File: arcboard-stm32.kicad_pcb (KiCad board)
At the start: 2 copper layers, 59.5 x 59.7 mm, 85 parts, among them J1 Conn_01x04_Socket, J10 Conn_01x04_Socket, J13 FFC05001-12SBA124W5M, J14 FFC05001-12SBA124W5M, J15 FFC05001-12SBA124W5M, J16 FFC05001-12SBA124W5M, J2 Conn_01x04_Socket, J3 FFC05001-12SBA124W5M, J4 FFC05001-12SBA124W5M, J5 Conn_01x02_Socket, J6 FFC05001-12SBA124W5M, J7 FFC05001-12SBA124W5M, J8 FFC05001-12SBA124W5M, J9 Conn_01x03_Socket, U1 XC6210B332MR-G, U10 1N4148W_C81598, U11 W25Q16JVSSIQTR, U13 2N7002, U15 TS-1187A-B-A-B, U2 TYPE-C-31-M-13, U3 STM32F405RGTx, U4 2N7002, U5 BAV70S,115, U6 BAV70S,115, U7 BAV70S,115, U8 BAV70S,115, U9 BAV70S,115, Y1 Crystal_GND24

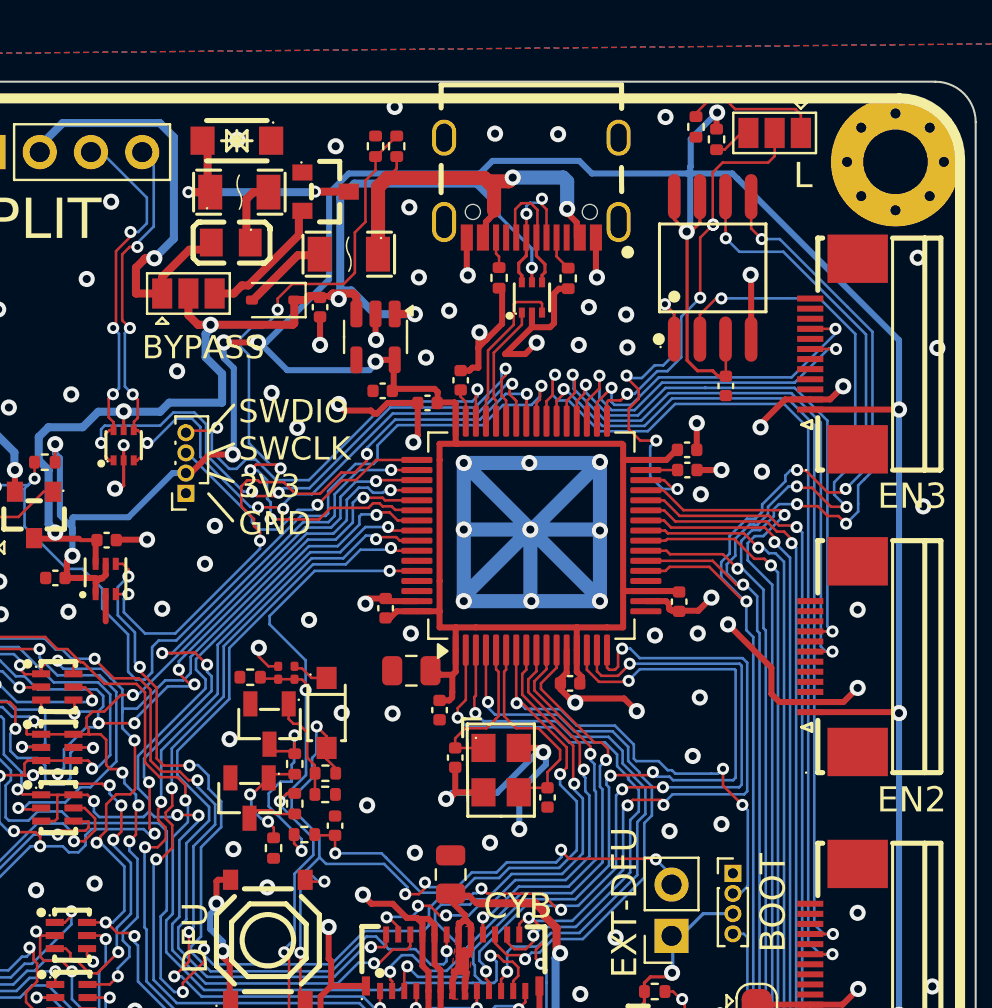
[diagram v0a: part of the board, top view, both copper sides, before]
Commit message: adding spare pins, more routing
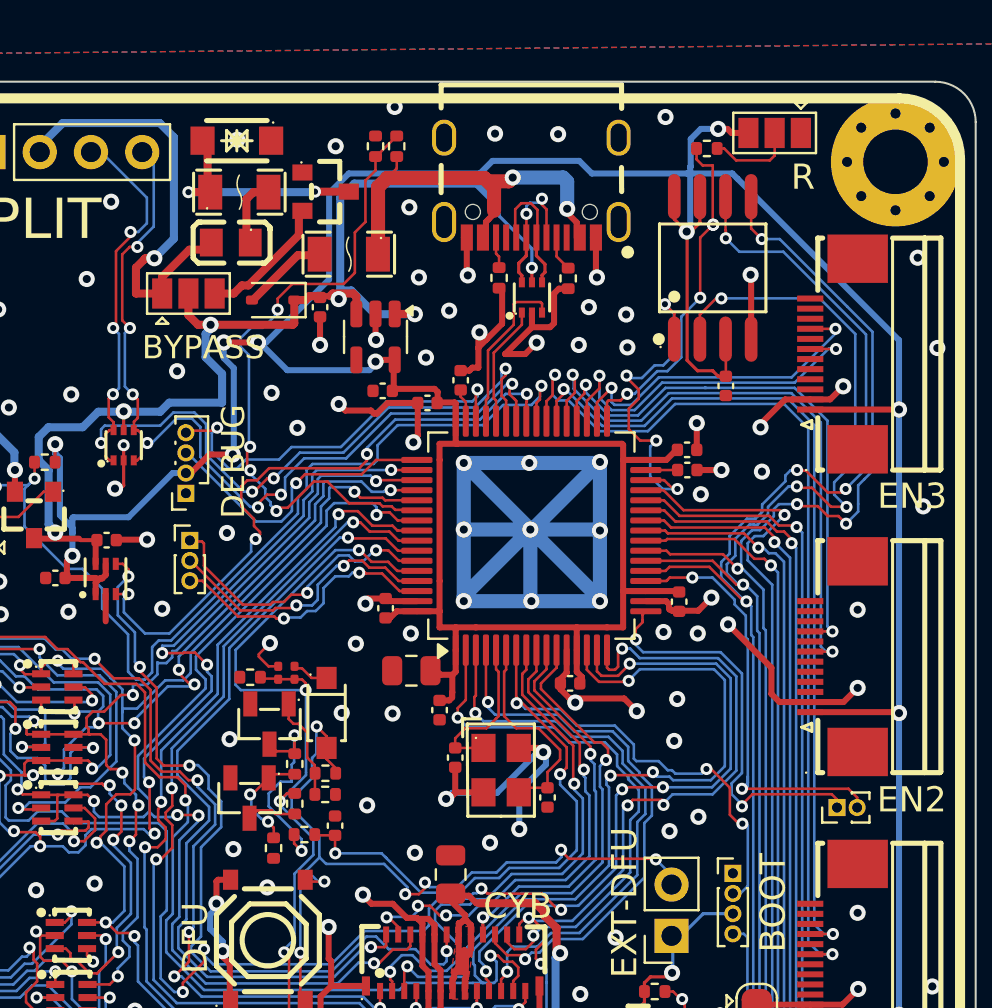
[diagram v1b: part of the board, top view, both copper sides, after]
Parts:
- removed R20: 10k, Resistor_SMD:R_0402_1005Metric
- added J11: Conn_01x02_Socket, Connector_PinHeader_1.00mm:PinHeader_1x02_P1.00mm_Vertical, F.Cu at (115.2, 98.5)
- added J12: Conn_01x03_Socket, Connector_PinHeader_1.00mm:PinHeader_1x03_P1.00mm_Vertical, F.Cu at (83.1, 85.2)
- moved R12 1.20 mm to (108.7, 65.8), turned to 180 degrees
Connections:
- JP3 pad 1: Net-(JP3-A) -> GND
- JP3 pad 2: SPLIT_HAND -> Net-(JP3-C)
- JP3 pad 3: Net-(JP3-B) -> +3V3
- R12 pad 1: GND -> Net-(JP3-C)
- R12 pad 2: Net-(JP3-A) -> SPLIT_HAND
- U3 pad 17: unconnected-(U3-PA3-Pad17) -> SPARE4
- U3 pad 20: unconnected-(U3-PA4-Pad20) -> SPARE5
- U3 pad 59: unconnected-(U3-PB7-Pad59) -> SPARE1
- U3 pad 61: unconnected-(U3-PB8-Pad61) -> SPARE2
- U3 pad 62: unconnected-(U3-PB9-Pad62) -> SPARE3
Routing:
- net SPARE5: track 0.00 -> 21.6 mm, vias 0 -> 2
- net SPARE4: track 0.00 -> 20.3 mm, vias 0 -> 2
- net SPARE1: track 0.00 -> 15.0 mm, vias 0 -> 2
- net SPARE2: track 0.00 -> 14.2 mm, vias 0 -> 2
- net SPARE3: track 0.00 -> 13.8 mm, vias 0 -> 2
- net Net-(JP3-A): track 6.86 -> 0.00 mm
- net BOOT0: track 90.6 -> 95.0 mm
- net Net-(JP3-C): track 0.00 -> 4.31 mm
- net SPLIT_HAND: track 20.1 -> 17.3 mm
- net VBUS_DETECT: track 35.0 -> 32.7 mm
- net ROW6: track 78.9 -> 76.8 mm
- net Net-(JP3-B): track 1.92 -> 0.00 mm
- net ROW5: track 128.4 -> 126.4 mm
- net ROW4: track 83.1 -> 81.4 mm
- net COL9: track 66.9 -> 68.3 mm
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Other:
- board text added: "DEBUG"
- board text added: "GND 3V3 SWCLK SWDIO"
- board text added: "R"
- board text removed: "L"
- board text removed: "SWDIO SWCLK 3V3 GND"

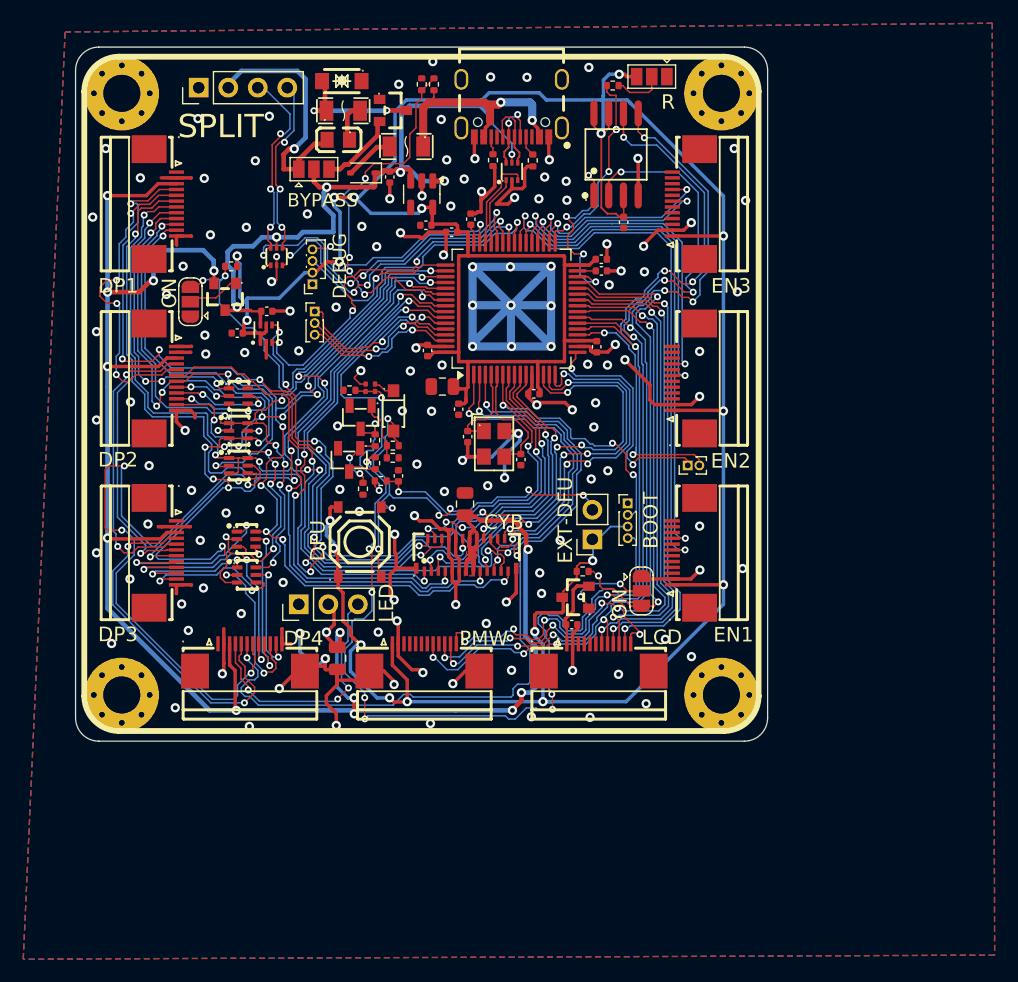
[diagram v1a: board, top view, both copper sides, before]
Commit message: silkscreen updates
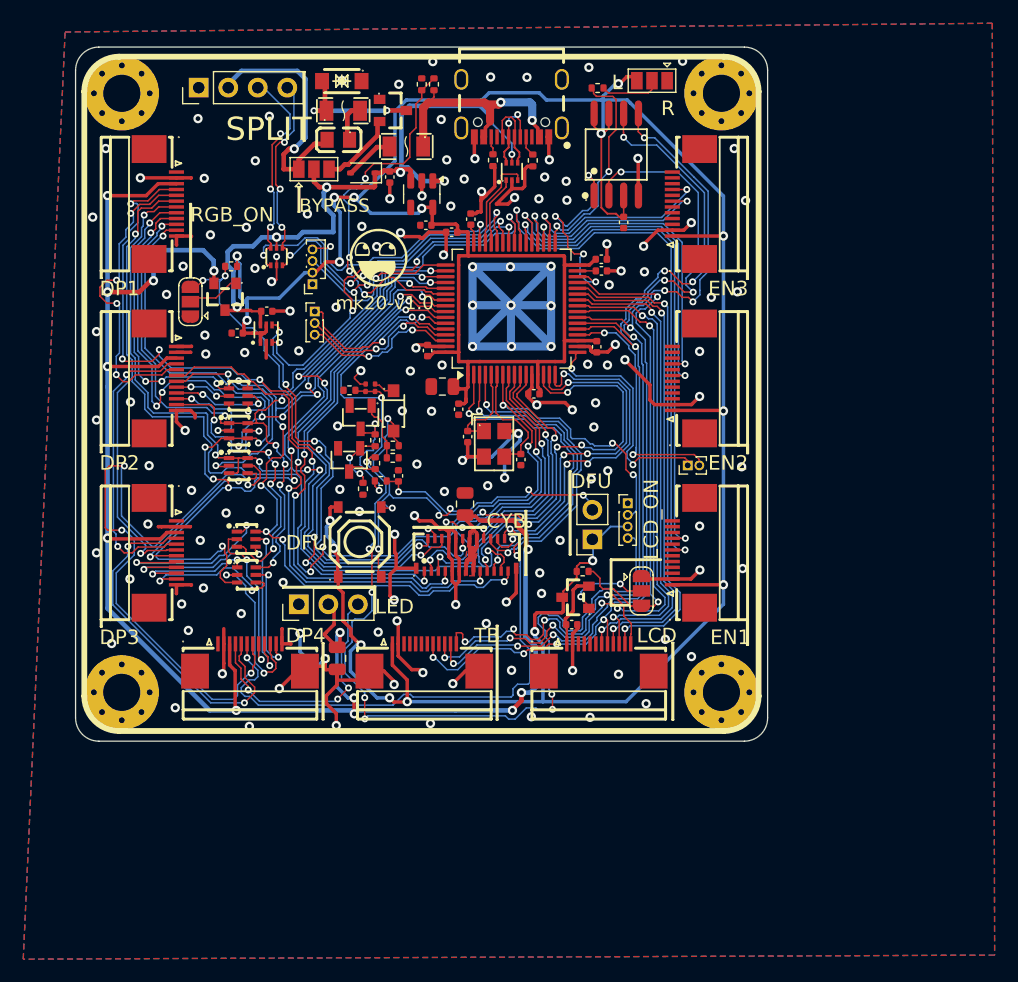
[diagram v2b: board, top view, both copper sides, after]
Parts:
- removed U11: W25Q16JVSSIQTR, kicad-libraries:SOIC-8_L5.3-W5.3-P1.27-LS8.0-BL
- added LOGO1: **REF, kicad-libraries:awesome-logo, B.Cu at (72.9, 95.7)
- added LOGO2: **REF, kicad-libraries:awesome-logo, F.Cu at (88.6, 80.6)
- added LOGO3: **REF, kicad-libraries:cyboard-logo-10mm, B.Cu at (96.2, 109.3)
- added LOGO4: **REF, kicad-libraries:qmk-lite, B.Cu at (105.1, 87.4)
- added U14: W25Q128JVSIQTR, kicad-libraries:SOIC-8_L5.3-W5.3-P1.27-LS8.0-BL, F.Cu at (109.0, 71.7)
- moved R12 1.32 mm to (107.4, 66.0)
- moved JP3 0.35 mm to (112.1, 65.4)
- moved H3 0.22 mm to (118.0, 118.0)
- moved H4 0.22 mm to (66.5, 118.0)
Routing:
- net ENCODER3_R2: track 16.8 -> 18.6 mm
- net GND: track 232.2 -> 234.0 mm, vias 141 -> 145
- net ENCODER2_R2: track 27.8 -> 29.4 mm
- net FLASH_CS: track 17.4 -> 19.0 mm
- net +3V3: track 290.9 -> 289.4 mm, vias 19 -> 18
- net ENCODER1_R1: track 46.1 -> 47.5 mm
- net COL10: track 96.8 -> 95.4 mm, vias 12 -> 11
- net ENCODER3_R1: track 18.1 -> 16.9 mm
- net RGB_ON: track 47.5 -> 48.7 mm
- net SPLIT_HAND: track 17.3 -> 18.5 mm, vias 4 -> 2
- net SPI1_CLK: track 87.6 -> 86.5 mm, vias 9 -> 8
- net ENCODER2_R1: track 30.2 -> 31.3 mm
- net Net-(JP3-C): track 4.31 -> 5.23 mm
- net Net-(J8-MOSI): track 14.8 -> 14.2 mm, vias 3 -> 2
- net LCD_ON: vias 3 -> 2
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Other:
- board text added: "51.55mm between holes"
- board text added: "59.5mm edge width"
- board text added: "59.7mm edge height"
- board text added: "DFU 3V3"
- board text added: "DO 5V GND"
- board text added: "GND NRST 3V3 BOOT0"
- board text added: "L"
- board text added: "LCD_ON"
- board text added: "LED-DO"
- board text added: "RGB_ON"
- board text added: "SPARE1 SPARE2 SPARE3"
- board text added: "SPARE5 SPARE4"
- board text added: "STM32-INATOR"
- board text added: "SWDIO SWCLK 3V3 GND"
- board text added: "TB"
- board text added: "mk20-v1.0"
- board text removed: "BOOT"
- board text removed: "DEBUG"
- board text removed: "DP1 = Dpad DP2-4 = Paddle EN1-2 = Top wheel encoders EN3 = Ring encoder CYB = Cyboard 25-pin LED = Gnd, +5v, WS2812 data ON = solder these for normal operation; else bypass EXT-DFU = activate DFU from external switch RESET = activate nRST from external switch BYPASS = solder arrow side to bypass R/L = handedness"
- board text removed: "EXT-DFU"
- board text removed: "GND 3V3 SWCLK SWDIO"
- board text removed: "ON"
- board text removed: "PMW"

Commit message: silkscreen improvements
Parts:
- added LOGO5: **REF, kicad-libraries:arcboard-stm32-qr-code-10x10, B.Cu at (115.3, 80.2)
- added LOGO6: **REF, kicad-libraries:cyboard-logo-5mm, F.Cu at (93.0, 102.2)
- moved LOGO3 30.6 mm to (106.6, 80.5)
- moved LOGO1 6.48 mm to (67.3, 92.4)
- moved LOGO2 5.91 mm to (88.9, 86.5)
- moved LOGO4 3.83 mm to (108.9, 87.1)
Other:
- board text added: "128MB"
- board text added: "STM32F405"

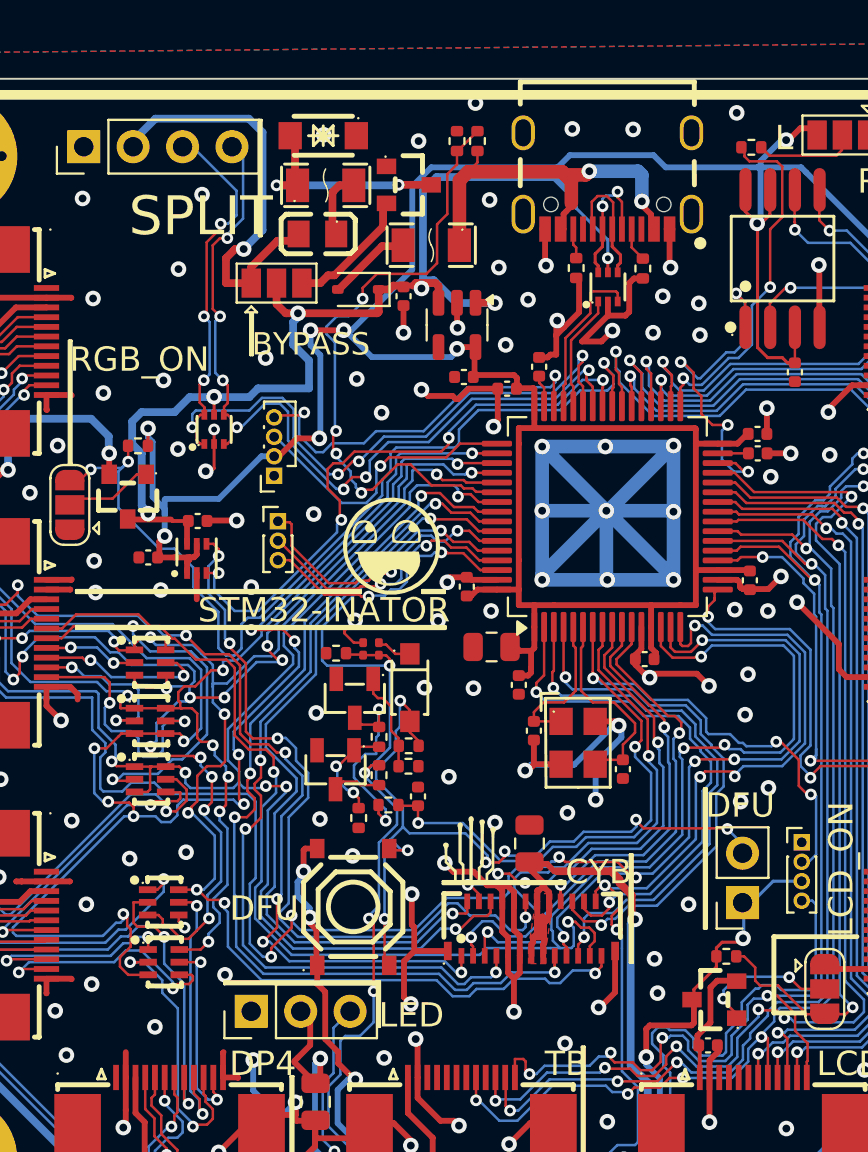
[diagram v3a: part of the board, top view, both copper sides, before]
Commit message: moved a few items, silkscreen improvements
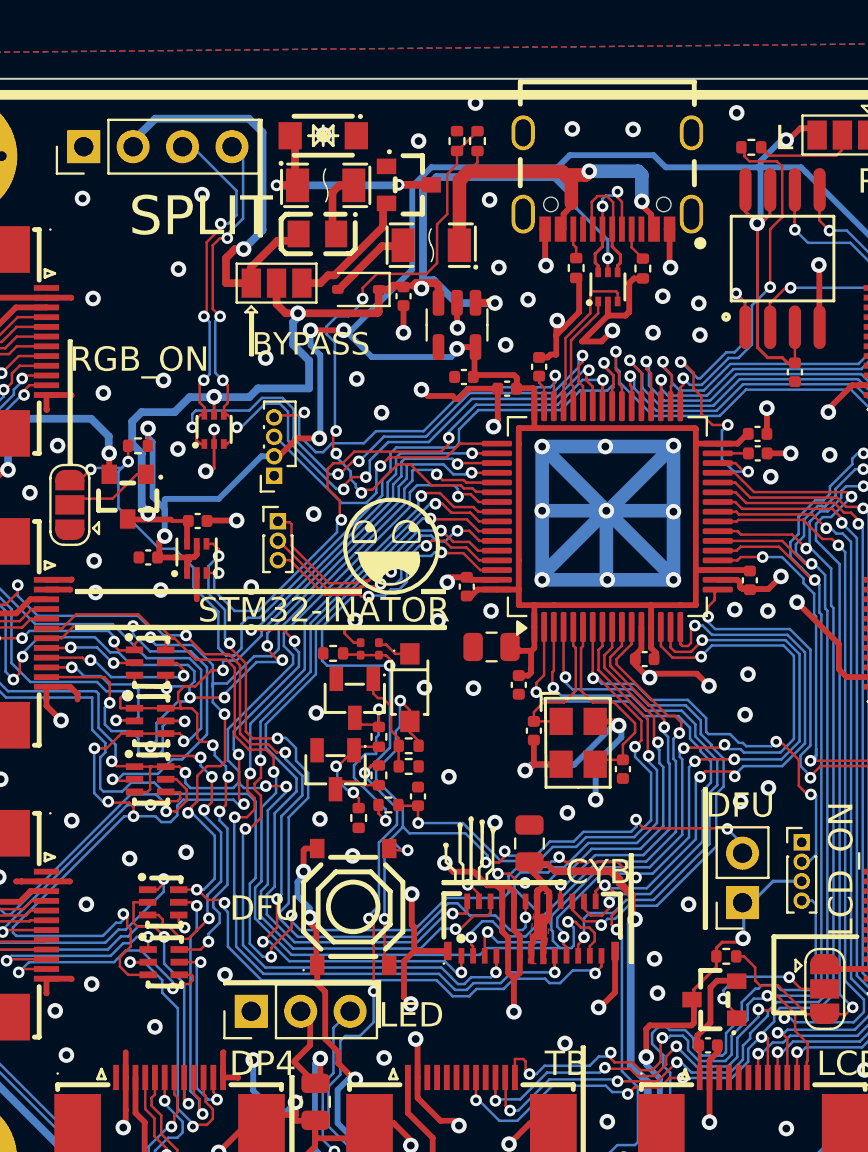
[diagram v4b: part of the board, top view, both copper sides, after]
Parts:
- removed R13: 0402WGF1002TCE, Resistor_SMD:R_0402_1005Metric
- added LOGO7: **REF, kicad-libraries:awesome-logo-25mm, B.Cu at (103.7, 85.5)
- added R16: 10k, Resistor_SMD:R_0402_1005Metric, F.Cu at (89.8, 97.8)
- R2, R3: value 0402WGF1002TCE -> 10k
- moved LOGO3 40.2 mm to (66.6, 84.0)
- moved LOGO5 34.4 mm to (104.1, 112.7)
- moved LOGO4 33.1 mm to (78.0, 99.0)
- moved LOGO1 10.9 mm to (68.9, 103.2)
- moved R3 2.14 mm to (88.3, 96.3), turned to -90 degrees
- moved R2 1.98 mm to (88.3, 98.3), turned to 90 degrees
- moved R1 0.15 mm to (85.9, 92.0)
- moved C22 0.13 mm to (87.3, 91.8)
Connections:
- R2 pad 1: Net-(U13-D) -> Net-(U4-D)
- R2 pad 2: Net-(U4-G) -> BOOT0
- R3 pad 1: Net-(U13-G) -> Net-(U13-D)
- R3 pad 2: GND -> Net-(U4-G)
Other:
- board text added: "51.55mm hole centers"
- board text removed: "51.55mm between holes"

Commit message: production version
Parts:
- removed R4, R5: 5.1k, Resistor_SMD:R_0402_1005Metric
- removed U2: TYPE-C-31-M-13, kicad-libraries:USB-C_SMD-TYPE-C-31-M-12
- added J17: Conn_01x04_Socket, Connector_JST:JST_XH_S4B-XH-A_1x04_P2.50mm_Horizontal, F.Cu at (95.8, 65.7)
- C22: footprint Capacitor_SMD:C_0201_0603Metric -> kicad-libraries:C0603
- R6: footprint Resistor_SMD:R_0201_0603Metric -> kicad-libraries:R0603
- moved U10 4.24 mm to (91.6, 97.7)
- moved D7 4.07 mm to (97.6, 76.5)
- moved C17 3.19 mm to (90.3, 102.6), turned to 90 degrees
- moved R16 2.79 mm to (90.2, 100.6)
- moved R15 2.78 mm to (89.8, 99.6)
- moved R6 2.67 mm to (88.7, 94.4), turned to 180 degrees
- moved R10 2.24 mm to (92.4, 67.7)
- moved U13 1.57 mm to (85.5, 94.5)
- moved R1 1.41 mm to (84.5, 92.0)
- moved F1 1.25 mm to (89.7, 70.9)
- moved R14 1.11 mm to (88.2, 100.8)
- moved C4 1.09 mm to (95.5, 77.0)
- moved R9 0.62 mm to (86.6, 100.5)
- moved U4 0.55 mm to (85.5, 98.0)
- moved C22 0.29 mm to (87.0, 91.9), turned to 0 degrees
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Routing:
- net FLASH_CS: track 19.0 -> 40.1 mm, vias 4 -> 2
- net +5V: track 60.8 -> 47.6 mm
- net GND: track 233.8 -> 222.3 mm, vias 145 -> 148
- net NRST: track 46.6 -> 55.3 mm
- net VBUS: track 23.5 -> 16.3 mm, vias 2 -> 1
- net +3V3: track 289.4 -> 295.5 mm, vias 18 -> 21
- net USB_DP: track 8.29 -> 2.25 mm
- net USB_CONN_DP: track 6.63 -> 11.7 mm, vias 0 -> 2
- net Net-(U13-G): track 5.17 -> 9.35 mm
- net USB_CONN_DM: track 6.94 -> 10.6 mm
- net BOOT0: track 95.0 -> 91.4 mm, vias 9 -> 10
- net ROW1: track 24.7 -> 27.4 mm
- net Net-(J5-Pin_2): track 41.1 -> 38.4 mm
- net SPI1_MISO: track 79.0 -> 81.7 mm
- net ENCODER2_R2: track 29.4 -> 27.4 mm
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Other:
- board text added: "MAIN"
- board text added: "VBS DP DM GND"
